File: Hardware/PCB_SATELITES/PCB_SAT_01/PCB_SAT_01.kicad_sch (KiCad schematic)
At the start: 40 parts, among them IC1 OPT3001DNPRQ1, IC2 OPT3001DNPRQ1, IC3 OPT3001DNPRQ1, IC4 OPT3001DNPRQ1

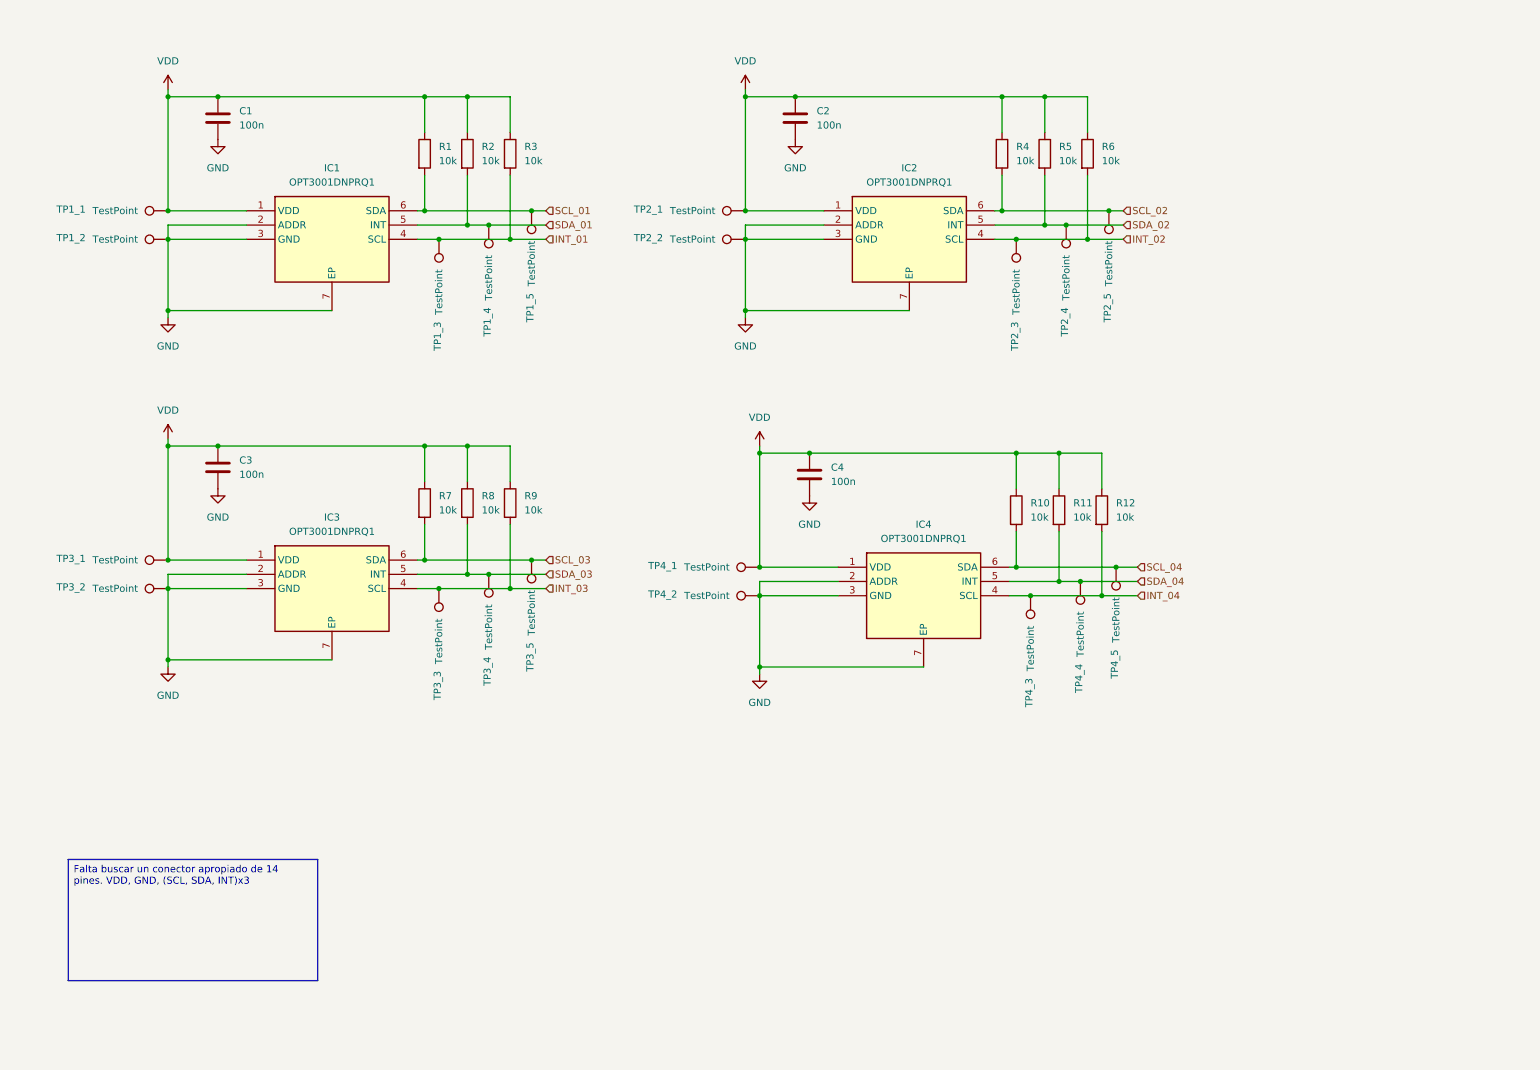
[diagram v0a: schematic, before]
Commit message: Actualizacion de PCB Satelite 01
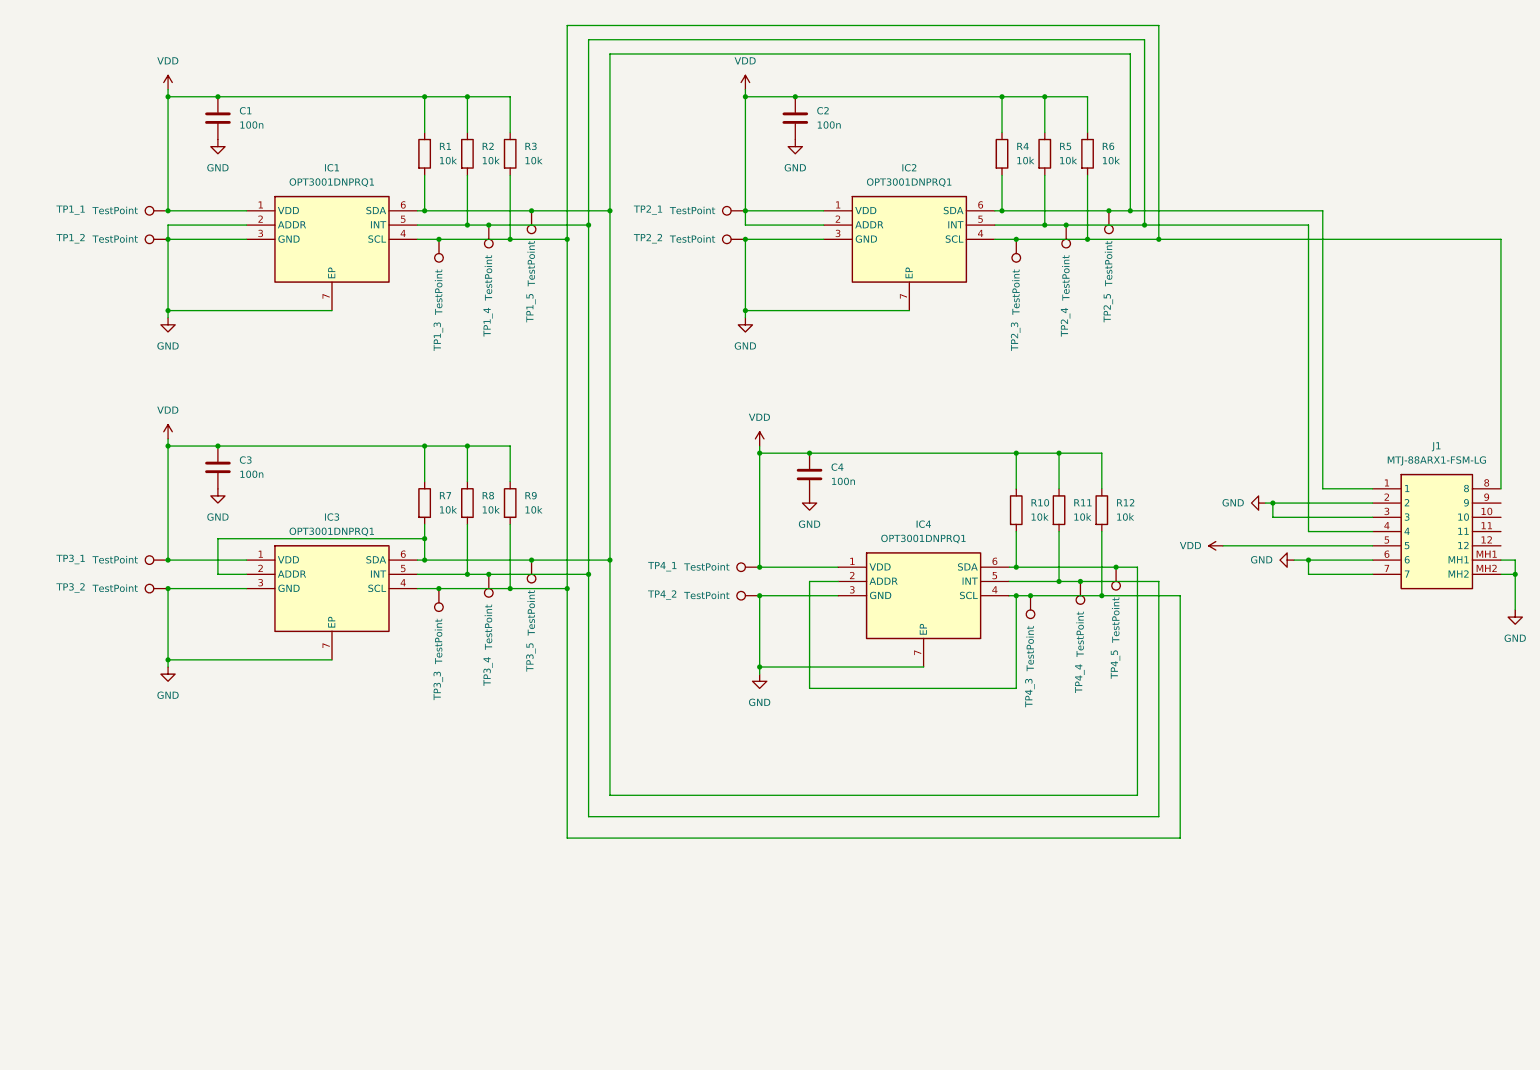
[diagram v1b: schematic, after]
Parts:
- added J1: MTJ-88ARX1-FSM-LG, MTJ88ARX1FSMLG, symbol MTJ-88ARX1-FSM-LG:MTJ-88ARX1-FSM-LG
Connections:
- net INT_02 is gone; now on an unnamed net: IC2.4 (SCL), R6.2, TP2_3.1
- net INT_03 is gone; now on an unnamed net: IC3.4 (SCL), R9.2, TP3_3.1
- net INT_04 is gone; now on an unnamed net: IC4.4 (SCL), R12.2, TP4_3.1
- net SCL_02 is gone; now on an unnamed net: IC2.6 (SDA), R4.2, TP2_5.1
- net SCL_03 is gone; now on an unnamed net: IC3.6 (SDA), R7.2, TP3_5.1
- net SCL_04 is gone; now on an unnamed net: IC4.6 (SDA), R10.2, TP4_5.1
- net SDA_02 is gone; now on an unnamed net: IC2.5 (INT), R5.2, TP2_4.1
- net SDA_03 is gone; now on an unnamed net: IC3.5 (INT), R8.2, TP3_4.1
- net SDA_04 is gone; now on an unnamed net: IC4.5 (INT), R11.2, TP4_4.1
- net GND: now also J1.2, J1.3, J1.6, J1.7, J1.MH1, J1.MH2; no longer IC2.2 (ADDR), IC3.2 (ADDR), IC4.2 (ADDR)
- net VDD: now also IC2.2 (ADDR), J1.5
- net INT_01: no longer names the net of IC1.4 (SCL), R3.2, TP1_3.1
- net INT_01: now also IC4.2 (ADDR), J1.8
- net SCL_01: no longer names the net of IC1.6 (SDA), R1.2, TP1_5.1
- net SCL_01: now also IC3.2 (ADDR), J1.1
- net SDA_01: no longer names the net of IC1.5 (INT), R2.2, TP1_4.1
- net SDA_01: now also J1.4

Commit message: Actualizacion PCB SATELITE 1
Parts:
- C1, C2, C3, C4: footprint (none) -> Capacitor_SMD:C_0805_2012Metric
- J1: footprint MTJ88ARX1FSMLG -> MTJ-88ARX1-FSM-LG:MTJ88ARX1FSMLG
- R1, R10, R11, R12, R2, R3, R4, R5, R6, R7, R8, R9: footprint (none) -> Resistor_SMD:R_0805_2012Metric
- TP1_1, TP1_2, TP1_3, TP1_4, TP1_5, TP2_1, TP2_2, TP2_3, TP2_4, TP2_5, TP3_1, TP3_2, TP3_3, TP3_4, TP3_5, TP4_1, TP4_2, TP4_3, TP4_4, TP4_5: footprint (none) -> TestPoint:TestPoint_Pad_D1.0mm
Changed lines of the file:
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@@
 			)
 		)
-		(property "Footprint" ""
+		(property "Footprint" "TestPoint:TestPoint_Pad_D1.0mm"
 			(at 143.51 41.91 0)
 			(effects
@@
 			)
 		)
-		(property "Footprint" ""
+		(property "Footprint" "TestPoint:TestPoint_Pad_D1.0mm"
 			(at 92.71 49.53 0)
 			(effects
@@
 			)
 		)
-		(property "Footprint" ""
+		(property "Footprint" "TestPoint:TestPoint_Pad_D1.0mm"
 			(at 100.33 109.22 0)
 			(effects
@@
 			)
 		)
-		(property "Footprint" ""
+		(property "Footprint" "Capacitor_SMD:C_0805_2012Metric"
 			(at 155.9052 97.79 0)
 			(effects
@@
 			)
 		)
-		(property "Footprint" ""
+		(property "Footprint" "TestPoint:TestPoint_Pad_D1.0mm"
 			(at 186.69 52.07 0)
 			(effects
@@
 			)
 		)
-		(property "Footprint" ""
+		(property "Footprint" "TestPoint:TestPoint_Pad_D1.0mm"
 			(at 40.64 104.14 0)
 			(effects
@@
 			)
 		)
-		(property "Footprint" ""
+		(property "Footprint" "Capacitor_SMD:C_0805_2012Metric"
 			(at 50.4952 34.29 0)
 			(effects
@@
 			)
 		)
-		(property "Footprint" ""
+		(property "Footprint" "TestPoint:TestPoint_Pad_D1.0mm"
 			(at 195.58 49.53 0)
 			(effects
@@
 			)
 		)
-		(property "Footprint" ""
+		(property "Footprint" "Resistor_SMD:R_0805_2012Metric"
 			(at 195.072 36.83 90)
 			(effects
@@
 			)
 		)
-		(property "Footprint" ""
+		(property "Footprint" "Resistor_SMD:R_0805_2012Metric"
 			(at 99.822 36.83 90)
 			(effects
@@
 			)
 		)
-		(property "Footprint" ""
+		(property "Footprint" "TestPoint:TestPoint_Pad_D1.0mm"
 			(at 83.82 114.3 0)
 			(effects
@@
 			)
 		)
-		(property "Footprint" ""
+		(property "Footprint" "Resistor_SMD:R_0805_2012Metric"
 			(at 187.452 36.83 90)
 			(effects
@@
 			)
 		)
-		(property "Footprint" ""
+		(property "Footprint" "Capacitor_SMD:C_0805_2012Metric"
 			(at 153.3652 34.29 0)
 			(effects
@@
 			)
 		)
-		(property "Footprint" ""
+		(property "Footprint" "TestPoint:TestPoint_Pad_D1.0mm"
 			(at 189.23 115.57 0)
 			(effects
@@
 			)
 		)
-		(property "Footprint" ""
+		(property "Footprint" "Resistor_SMD:R_0805_2012Metric"
 			(at 92.202 99.06 90)
 			(effects
@@
 			)
 		)
-		(property "Footprint" ""
+		(property "Footprint" "Resistor_SMD:R_0805_2012Metric"
 			(at 189.992 100.33 90)
 			(effects
@@
 			)
 		)
-		(property "Footprint" ""
+		(property "Footprint" "Resistor_SMD:R_0805_2012Metric"
 			(at 92.202 36.83 90)
 			(effects
@@
 			)
 		)
-		(property "Footprint" ""
+		(property "Footprint" "TestPoint:TestPoint_Pad_D1.0mm"
 			(at 203.2 46.99 0)
 			(effects
@@
 			)
 		)
-		(property "Footprint" ""
+		(property "Footprint" "TestPoint:TestPoint_Pad_D1.0mm"
 			(at 100.33 46.99 0)
 			(effects
@@
 			)
 		)
-		(property "Footprint" ""
+		(property "Footprint" "TestPoint:TestPoint_Pad_D1.0mm"
 			(at 92.71 111.76 0)
 			(effects
@@
 			)
 		)
-		(property "Footprint" ""
+		(property "Footprint" "TestPoint:TestPoint_Pad_D1.0mm"
 			(at 40.64 109.22 0)
 			(effects
@@
 			)
 		)
-		(property "Footprint" ""
+		(property "Footprint" "TestPoint:TestPoint_Pad_D1.0mm"
 			(at 143.51 46.99 0)
 			(effects
@@
 			)
 		)
-		(property "Footprint" ""
+		(property "Footprint" "Capacitor_SMD:C_0805_2012Metric"
 			(at 50.4952 96.52 0)
 			(effects
@@
 			)
 		)
-		(property "Footprint" ""
+		(property "Footprint" "TestPoint:TestPoint_Pad_D1.0mm"
 			(at 83.8347 52.07 0)
 			(effects
@@
 			)
 		)
-		(property "Footprint" ""
+		(property "Footprint" "Resistor_SMD:R_0805_2012Metric"
 			(at 205.232 100.33 90)
 			(effects
@@
 			)
 		)
-		(property "Footprint" "MTJ88ARX1FSMLG"
+		(property "Footprint" "MTJ-88ARX1-FSM-LG:MTJ88ARX1FSMLG"
 			(at 274.32 191.44 0)
 			(effects
@@
 			)
 		)
-		(property "Footprint" ""
+		(property "Footprint" "TestPoint:TestPoint_Pad_D1.0mm"
 			(at 146.05 105.41 0)
 			(effects
@@
 			)
 		)
-		(property "Footprint" ""
+		(property "Footprint" "TestPoint:TestPoint_Pad_D1.0mm"
 			(at 198.12 113.03 0)
 			(effects
@@
 			)
 		)
-		(property "Footprint" ""
+		(property "Footprint" "Resistor_SMD:R_0805_2012Metric"
 			(at 84.582 99.06 90)
 			(effects
@@
 			)
 		)
-		(property "Footprint" ""
+		(property "Footprint" "TestPoint:TestPoint_Pad_D1.0mm"
 			(at 40.64 41.91 0)
 			(effects
@@
 			)
 		)
-		(property "Footprint" ""
+		(property "Footprint" "Resistor_SMD:R_0805_2012Metric"
 			(at 197.612 100.33 90)
 			(effects
@@
 			)
 		)
-		(property "Footprint" ""
+		(property "Footprint" "Resistor_SMD:R_0805_2012Metric"
 			(at 84.582 36.83 90)
 			(effects
@@
 			)
 		)
-		(property "Footprint" ""
+		(property "Footprint" "TestPoint:TestPoint_Pad_D1.0mm"
 			(at 204.47 110.49 0)
 			(effects
@@
 			)
 		)
-		(property "Footprint" ""
+		(property "Footprint" "Resistor_SMD:R_0805_2012Metric"
 			(at 202.692 36.83 90)
 			(effects
@@
 			)
 		)
-		(property "Footprint" ""
+		(property "Footprint" "TestPoint:TestPoint_Pad_D1.0mm"
 			(at 146.05 110.49 0)
 			(effects
@@
 			)
 		)
-		(property "Footprint" ""
+		(property "Footprint" "TestPoint:TestPoint_Pad_D1.0mm"
 			(at 40.64 46.99 0)
 			(effects
@@
 			)
 		)
-		(property "Footprint" ""
+		(property "Footprint" "Resistor_SMD:R_0805_2012Metric"
 			(at 99.822 99.06 90)
 			(effects

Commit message: Actualizacion PCB SATELITE 1
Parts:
- removed R10, R11, R12, R4, R5, R6, R7, R8, R9: 10k, Resistor_SMD:R_0805_2012Metric, symbol Device:R
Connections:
- net GND: now also J1.8; no longer J1.6
- net SCL: now reaches IC1.4 (SCL), IC2.4 (SCL), IC3.4 (SCL), IC4.2 (ADDR), IC4.4 (SCL), R3.2, TP1_3.1, TP2_3.1, TP3_3.1, TP4_3.1
- net SCL: now also J1.6; no longer J1.8
- net INT: now reaches IC1.5 (INT), IC2.5 (INT), IC3.5 (INT), IC4.5 (INT), J1.4, R2.2, TP1_4.1, TP2_4.1, TP3_4.1, TP4_4.1
- net SDA: now reaches IC1.6 (SDA), IC2.6 (SDA), IC3.2 (ADDR), IC3.6 (SDA), IC4.6 (SDA), J1.1, R1.2, TP1_5.1, TP2_5.1, TP3_5.1, TP4_5.1
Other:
- note added: "RJ45 CONECTOR FEMALE"
- note added: "SENSOR 1 ADDRESS: 1000 100"
- note added: "SENSOR 2 ADDRESS: 1000 101"
- note added: "SENSOR 3 ADDRESS: 1000 110"
- note added: "SENSOR 4 ADDRESS: 1000 111"
- moved on the sheet: C1, C2, C3, C4, IC1, IC2, IC3, IC4, J1, R1, R2, R3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

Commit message: Actualizacion PCB SATELITE 1
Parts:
- removed C2, C3, C4: 100n, Capacitor_SMD:C_0805_2012Metric, symbol Device:C
- removed TP2_1, TP2_2, TP2_3, TP2_4, TP2_5, TP3_1, TP3_2, TP3_3, TP3_4, TP3_5, TP4_1, TP4_2, TP4_3, TP4_4, TP4_5: TestPoint, TestPoint:TestPoint_Pad_D1.0mm, symbol Connector:TestPoint
- renumbered TP1_2 to TP_GND1, TP1_5 to TP_INT1, TP1_4 to TP_SCL1, TP1_3 to TP_SDA1, TP1_1 to TP_VDD1
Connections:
- net INT: now also TP_INT1.1; no longer TP_SCL1.1
- net SCL: now also TP_SCL1.1; no longer TP_SDA1.1
- net SDA: now also TP_SDA1.1; no longer TP_INT1.1
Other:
- note added: "TEST POINTs"
- moved on the sheet: TP_GND1, TP_INT1, TP_SCL1, TP_SDA1, TP_VDD1

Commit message: actualizacion pcb satelite
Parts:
- added C2, C3, C4: 100n, Capacitor_SMD:C_0805_2012Metric, symbol Device:C
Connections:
- net GND: now also C2.2, C3.2, C4.2
- net VDD: now also C2.1, C3.1, C4.1
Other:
- moved on the sheet: C1
